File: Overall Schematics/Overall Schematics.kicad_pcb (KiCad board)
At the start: 2 copper layers, 152.4 x 152.4 mm, 28 parts, among them J1 WattMeter1_Output, J2 WattMeter2_Output, J3 Intel_Buck_Converter_Input, J4 WattMeter1_Input, J5 WattMeter2_Input, M1 Stepper_Motor_bipolar, M2 Stepper_Motor_bipolar, M3 LinActuator12V, M4 LinActuator12V, M5 LinActuator12V, M6 Motor_DC, M7 Motor_DC, M8 Motor_DC, M9 Motor_DC, SW1 SW_DPST, U1 Teensy4.1, U10 VNH52019, U12 36v4SMD, U2 36v4SMD, U3 36v4SMD, U4 VNH52019, U5 VNH52019, U6 VNH52019, U7 VNH52019, U8 VNH52019, U9 VNH52019

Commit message: flipped some screw terminals and added screw terminal
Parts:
- added M11: Stepper_Motor_bipolar, TerminalBlock:TerminalBlock_bornier-4_P5.08mm, B.Cu at (459.7, 375.9)
- BT1, BT2, J3: moved to B.Cu
- moved BT2 160.6 mm to (515.6, 429.3), turned to 90 degrees
- moved BT1 144.2 mm to (528.3, 429.3), turned to 90 degrees
- moved J5 99.7 mm to (602.0, 410.2)
- moved J3 95.6 mm to (577.9, 431.8), turned to 90 degrees
- moved M3 83.6 mm to (476.2, 459.7), turned to 180 degrees
- moved M5 48.5 mm to (459.7, 396.2), turned to 270 degrees
- moved M6 35.9 mm to (459.7, 434.3), turned to 270 degrees
- moved M9 35.6 mm to (577.9, 452.1), turned to 90 degrees
- moved M8 34.2 mm to (576.6, 416.6), turned to 90 degrees
- moved M4 33.0 mm to (458.5, 322.6), turned to 0 degrees
- moved M7 32.2 mm to (576.6, 396.2), turned to 90 degrees
- moved M2 32.2 mm to (576.6, 365.8)
- moved M1 30.6 mm to (576.6, 327.7)

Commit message: PCB Updates
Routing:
- net OUTB1_LIN: track 0.00 -> 15.2 mm
- net OUTA1_LIN: track 0.00 -> 15.2 mm
- net AOUT1_3: track 0.00 -> 12.2 mm
- net AOUT2_3: track 0.00 -> 11.9 mm
- net BOUT1_3: track 0.00 -> 10.1 mm
- net BOUT2_3: track 0.00 -> 9.06 mm
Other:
- net class Power: trace_width 0.5 -> 0.75

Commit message: PCB Updates
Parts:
- added M10: Motor_Servo, TerminalBlock:TerminalBlock_bornier-3_P5.08mm, B.Cu at (528.3, 461.0)
- added U11: ServoDriver, Custom Footprints:ServoMotorDriver, F.Cu at (539.5, 452.2)
- moved M3 1.27 mm to (475.0, 459.7)
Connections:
- U1 pad 17: LIN_SIGNAL1 -> LIN_SIGNAL3
- U1 pad 18: LIN_SIGNAL2 -> LIN_SIGNAL1
- U1 pad 19: LIN_SIGNAL3 -> LIN_SIGNAL2
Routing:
- net LIN_SIGNAL2: track 0.00 -> 170.1 mm
- net LIN_SIGNAL1: track 0.00 -> 81.7 mm
- net LIN_SIGNAL3: track 0.00 -> 61.4 mm
- net OUTB_3: track 0.00 -> 52.0 mm
- net OUTA_3: track 0.00 -> 51.0 mm
- net OUTA2_LIN: track 0.00 -> 44.6 mm
- net OUTA_4: track 0.00 -> 42.6 mm
- net OUTB_4: track 0.00 -> 41.6 mm
- net OUTB2_LIN: track 0.00 -> 38.2 mm
- net OUTB3_LIN: track 0.00 -> 22.4 mm
- net AOUT1_2: track 0.00 -> 17.2 mm
- net AOUT1_1: track 0.00 -> 15.8 mm
- net OUTA_1: track 0.00 -> 15.4 mm
- net OUTB_1: track 0.00 -> 15.4 mm
- net OUTA3_LIN: track 0.00 -> 14.2 mm
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
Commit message: did some pcb stuff
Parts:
- removed BT1: True_Spec_Battery1, Custom Footprints:AMASS_XT60-F_1x02_P7.20mm_Vertical
- removed BT2: True_Spec_Battery2, Custom Footprints:AMASS_XT60-F_1x02_P7.20mm_Vertical
- removed J4: WattMeter1_Input, TerminalBlock:TerminalBlock_bornier-2_P5.08mm
- removed J5: WattMeter2_Input, TerminalBlock:TerminalBlock_bornier-2_P5.08mm
- removed SW1: SW_DPST, Button_Switch_SMD:SW_MEC_5GSH9
- added M12: Motor_Servo, TerminalBlock:TerminalBlock_bornier-3_P5.08mm, B.Cu at (532.8, 447.7)
- J1, J2: moved to B.Cu
- moved J2 214.6 mm to (518.2, 424.8)
- moved J1 214.3 mm to (518.2, 393.1)
- moved M10 5.12 mm to (532.8, 458.5)
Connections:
- net Battery1_Positive renamed Battery2_Positive
- net Net-(M10-Pad1) renamed SS_1
- J2 pad 2: Battery1_Positive24V -> Battery2_Positive24V
- M10 pad 2: Net-(M10-Pad2) -> +5V
- M10 pad 3: Net-(M10-Pad3) -> GND
- U11 pad 13: Net-(M10-Pad3) -> GND
- U11 pad 14: Net-(U11-Pad14) -> GND
- U11 pad 2: Net-(U11-Pad2) -> SS_2
- U11 pad 7: Net-(M10-Pad2) -> +5V
- U11 pad 8: Net-(U11-Pad8) -> +5V
- U12 pad 17: Battery1_Positive24V -> Battery2_Positive24V
- U12 pad 18: Battery1_Positive24V -> Battery2_Positive24V
- U2 pad 17: Battery1_Positive24V -> Battery2_Positive24V
- U2 pad 18: Battery1_Positive24V -> Battery2_Positive24V
- U5 pad 14: Battery1_Positive24V -> Battery2_Positive24V
- U7 pad 14: Battery1_Positive24V -> Battery2_Positive24V
- U8 pad 14: Battery1_Positive24V -> Battery2_Positive24V
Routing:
- net +5V: track 0.00 -> 35.3 mm
- net LIN_SIGNAL2: track 170.1 -> 141.4 mm
- net SS_1: track 0.00 -> 25.8 mm
- net SS_2: track 0.00 -> 25.6 mm
- net OUTA2_LIN: track 44.6 -> 38.4 mm
- net OUTB2_LIN: track 38.2 -> 32.7 mm
- net AOUT1_2: track 17.2 -> 14.2 mm
- net OUTB3_LIN: track 22.4 -> 20.1 mm
- net AOUT1_1: track 15.8 -> 13.8 mm
- net OUTA3_LIN: track 14.2 -> 13.0 mm
- net OUTA_4: track 42.6 -> 41.6 mm
- net AOUT2_3: track 11.9 -> 11.2 mm
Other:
- net class Power: trace_width 0.75 -> 1
- net class Signal: trace_width 0.25 -> 0.5

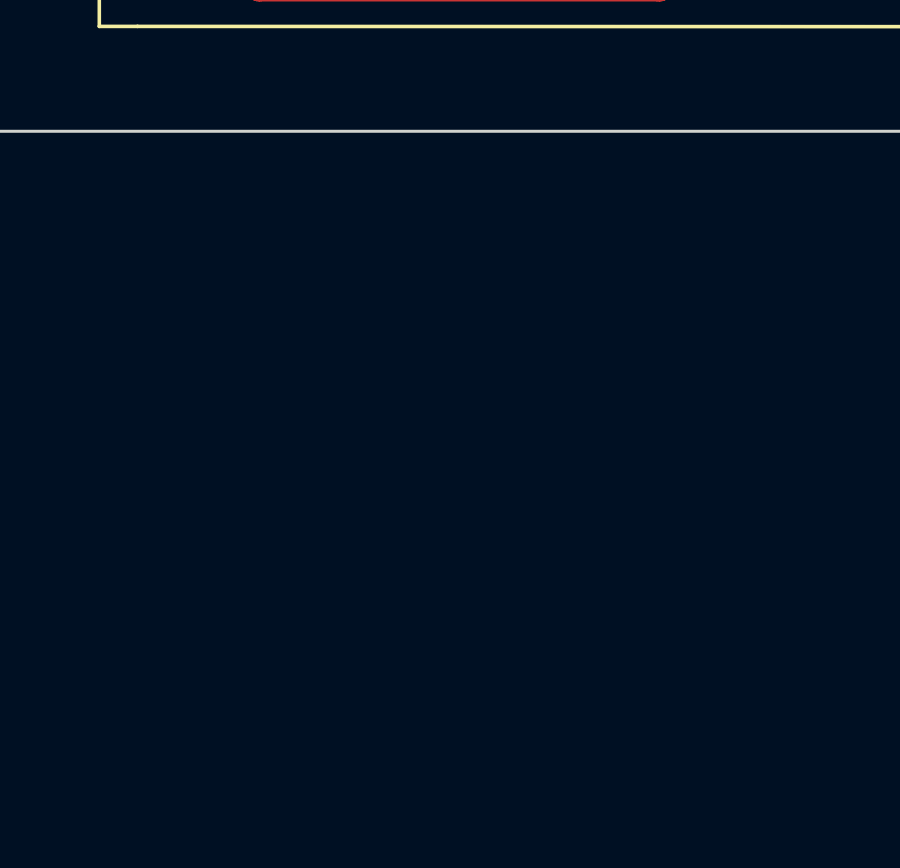
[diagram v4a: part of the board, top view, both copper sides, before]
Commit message: Added 5V buck
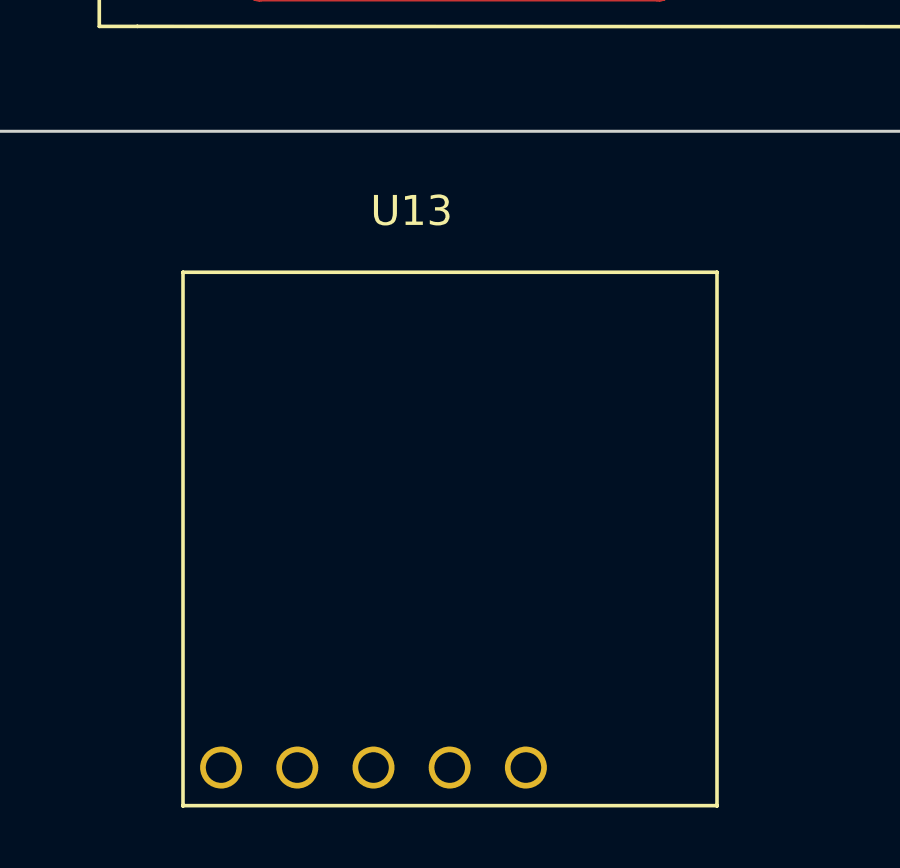
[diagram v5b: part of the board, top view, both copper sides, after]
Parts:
- added U13: D24V22F5, Custom Footprints:D24V22F5, F.Cu at (515.6, 469.3)
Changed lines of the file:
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@@
     (tracks 269)
     (zones 0)
-    (modules 27)
+    (modules 28)
     (nets 159)
   )
@@
     )
   )
+  (module "Custom Footprints:D24V22F5" (layer F.Cu)
+    (at 515.62 469.265)
+    (fp_text reference U13 (at 0 0.5) (layer F.SilkS)
+      (effects (font (size 1 1) (thickness 0.15)))
+    )
+    (fp_text value D24V22F5 (at 0 -0.5) (layer F.Fab)
+      (effects (font (size 1 1) (thickness 0.15)))
+    )
+    (fp_line (start -7.62 20.32) (end 10.18 20.32) (layer F.SilkS) (width 0.12))
+    (fp_line (start 10.18 2.54) (end 10.18 20.34) (layer F.SilkS) (width 0.12))
+    (fp_line (start -7.62 2.54) (end 10.18 2.54) (layer F.SilkS) (width 0.12))
+    (fp_line (start -7.62 2.54) (end -7.62 20.34) (layer F.SilkS) (width 0.12))
+    (pad 1 thru_hole circle (at -6.35 19.05) (size 1.4 1.4) (drill 1.02) (layers *.Cu *.Mask))
+    (pad 2 thru_hole circle (at -3.81 19.05) (size 1.4 1.4) (drill 1.02) (layers *.Cu *.Mask))
+    (pad 3 thru_hole circle (at -1.27 19.05) (size 1.4 1.4) (drill 1.02) (layers *.Cu *.Mask))
+    (pad 4 thru_hole circle (at 1.27 19.05) (size 1.4 1.4) (drill 1.02) (layers *.Cu *.Mask))
+    (pad 5 thru_hole circle (at 3.81 19.05) (size 1.4 1.4) (drill 1.02) (layers *.Cu *.Mask))
+  )
   (gr_line (start 592.074 314.706) (end 592.1 467.106) (layer Edge.Cuts) (width 0.1))

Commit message: PCB is basically done, going to check stuff again before ordering though
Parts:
- moved J2 105.1 mm to (543.6, 322.8)
- moved J1 73.7 mm to (495.8, 322.8)
- moved U13 33.5 mm to (497.2, 441.3)
- moved M10 5.72 mm to (538.5, 458.5)
- moved M12 5.72 mm to (538.5, 447.7)
- moved U11 5.72 mm to (545.2, 452.2)
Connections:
- J3 pad 1: Battery2_Positive -> Battery2_Positive24V
- U10 pad 14: Battery1_Positive24V -> Battery2_Positive24V
- U12 pad 17: Battery2_Positive24V -> Battery1_Positive24V
- U12 pad 18: Battery2_Positive24V -> Battery1_Positive24V
- U13 pad 1: (no net) -> Net-(U13-Pad1)
- U13 pad 2: (no net) -> Net-(U13-Pad2)
- U13 pad 3: (no net) -> Battery1_Positive24V
- U13 pad 4: (no net) -> GND
- U13 pad 5: (no net) -> +5V
- U3 pad 17: Battery1_Positive24V -> Battery2_Positive24V
- U3 pad 18: Battery1_Positive24V -> Battery2_Positive24V
- U5 pad 14: Battery2_Positive24V -> Battery1_Positive24V
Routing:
- net +3V3: track 0.00 -> 475.4 mm, vias 0 -> 1
- net Battery1_Positive24V: track 0.00 -> 293.3 mm
- net Battery2_Positive24V: track 0.00 -> 249.6 mm
- net +5V: track 35.3 -> 50.6 mm
- net PWM_4: track 38.3 -> 43.7 mm
- net DIR_1: track 30.6 -> 36.0 mm
- net STEP_1: track 30.6 -> 35.4 mm
- net PWM_7: track 26.9 -> 29.7 mm
- net INA_7: track 28.0 -> 30.5 mm
- net OUTB2_LIN: track 32.7 -> 31.2 mm
- net LIN_SIGNAL2: track 141.4 -> 139.9 mm
- net INA_4: track 35.9 -> 37.1 mm
- net INB_4: track 25.8 -> 27.0 mm
- net INA_3: track 50.4 -> 49.3 mm
- net INB_3: track 67.5 -> 66.4 mm
- added copper zone on F.Cu, net GND
- added copper zone on B.Cu, net PWR_GND
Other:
- net class Power: via_dia 0.8 -> 1.2; via_drill 0.4 -> 0.8

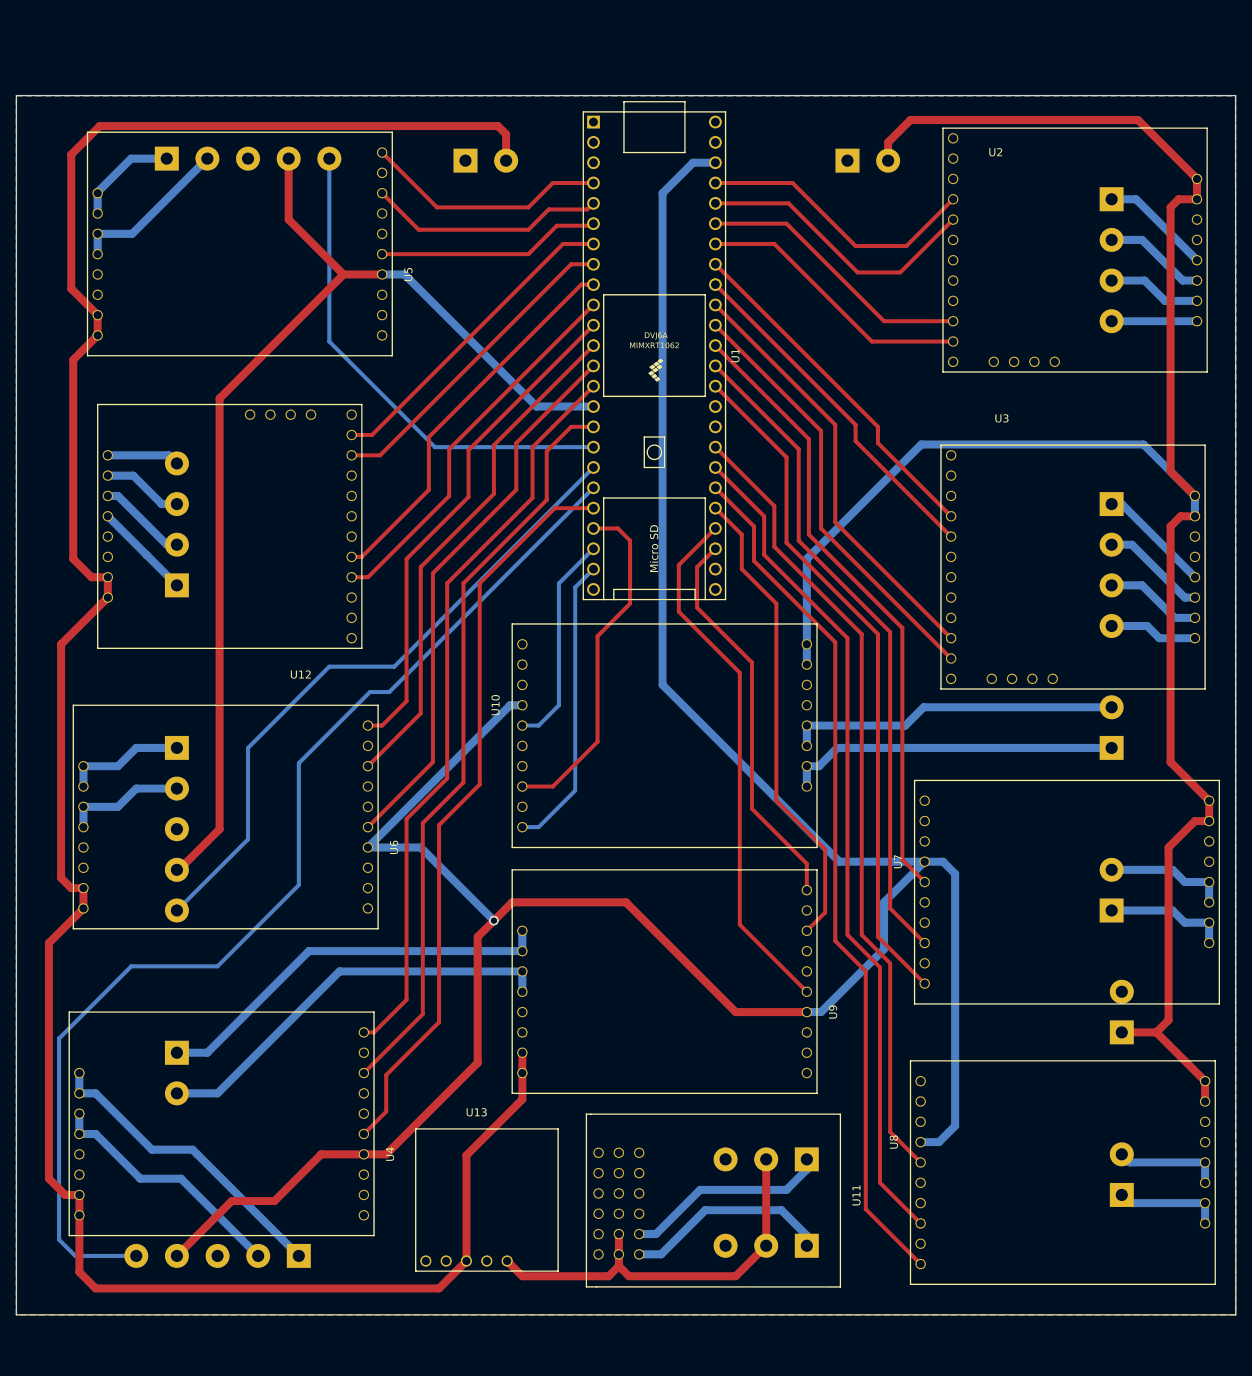
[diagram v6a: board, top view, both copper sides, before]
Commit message: Added mounting, add to make board a bit bigger. Changed servo screw terminal pitch to 2.54mm
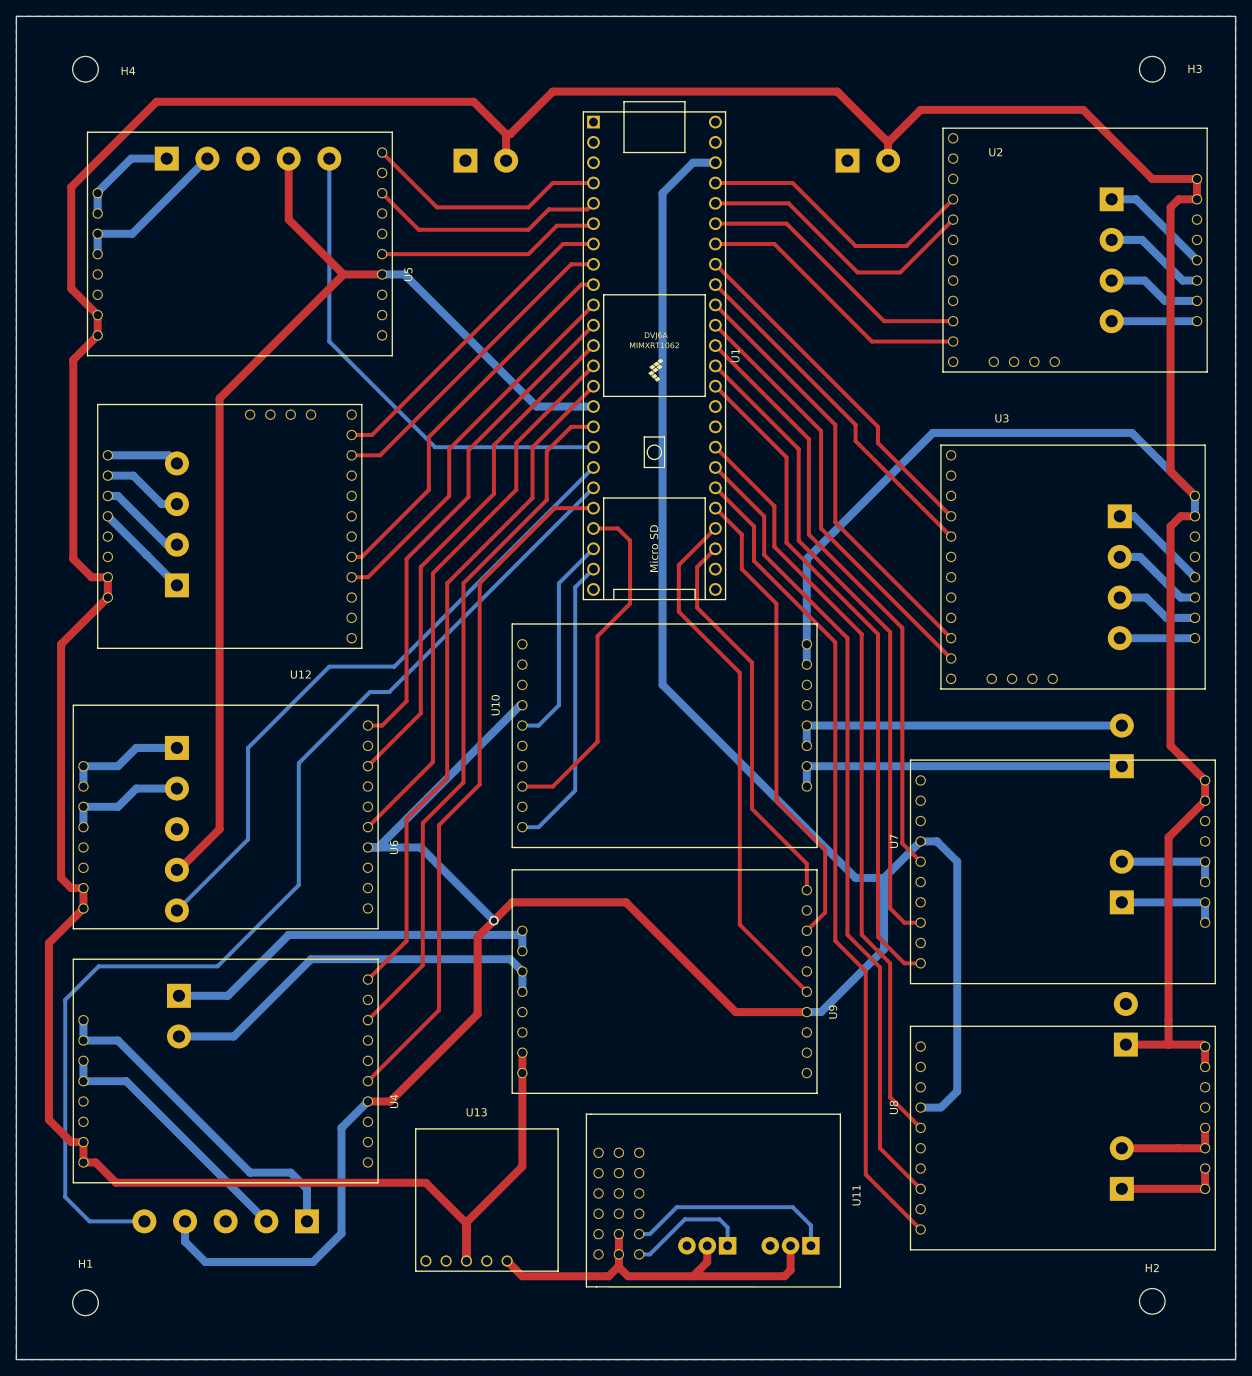
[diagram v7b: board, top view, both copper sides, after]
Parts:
- added H1: MountingHole, MountingHole:MountingHole_3.2mm_M3, F.Cu at (448.3, 465.6)
- added H2: MountingHole, MountingHole:MountingHole_3.2mm_M3, F.Cu at (581.7, 465.5)
- added H3: MountingHole, MountingHole:MountingHole_3.2mm_M3, F.Cu at (581.7, 311.4)
- added H4: MountingHole, MountingHole:MountingHole_3.2mm_M3, F.Cu at (448.3, 311.4)
- M10, M12: footprint TerminalBlock:TerminalBlock_bornier-3_P5.08mm -> Custom Footprints:TerminalBlock_2.54_1x03_P2.54mm_Horizontal
- moved M12 10.8 mm to (539.0, 458.5)
- moved M10 9.91 mm to (528.6, 458.5)
- moved M6 7.12 mm to (460.0, 427.2)
- moved U4 6.62 mm to (487.4, 440.4)
- moved M3 4.44 mm to (476.0, 455.4)
- moved U8 4.32 mm to (548.9, 441.2)
- moved M7 2.62 mm to (577.9, 398.5)
- moved U7 2.59 mm to (548.9, 407.9)
- moved M2 1.83 mm to (577.6, 367.3)
- moved M8 1.63 mm to (577.9, 415.5)
- moved J3 1.61 mm to (578.4, 433.3)
- moved M9 0.76 mm to (577.9, 451.4)
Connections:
- net +3V3 renamed 3.3V
- J2 pad 2: Battery2_Positive24V -> Battery1_Positive24V
- J3 pad 1: Battery2_Positive24V -> Battery1_Positive24V
- U10 pad 14: Battery2_Positive24V -> Battery1_Positive24V
- U2 pad 17: Battery2_Positive24V -> Battery1_Positive24V
- U2 pad 18: Battery2_Positive24V -> Battery1_Positive24V
- U3 pad 17: Battery2_Positive24V -> Battery1_Positive24V
- U3 pad 18: Battery2_Positive24V -> Battery1_Positive24V
- U7 pad 14: Battery2_Positive24V -> Battery1_Positive24V
- U8 pad 14: Battery2_Positive24V -> Battery1_Positive24V
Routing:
- net Battery1_Positive24V: track 293.3 -> 585.9 mm
- net Battery2_Positive24V: track 249.6 -> 0.00 mm
- net SS_1: track 25.8 -> 15.6 mm
- net INA_6: track 93.4 -> 85.8 mm
- net PWM_6: track 94.3 -> 87.5 mm
- net INB_6: track 92.9 -> 86.1 mm
- net INA_2: track 107.7 -> 103.3 mm
- net PWM_2: track 105.1 -> 100.8 mm
- net INB_2: track 100.0 -> 95.7 mm
- net OUTA2_LIN: track 38.4 -> 42.2 mm
- net 3.3V: track 475.4 -> 479.0 mm
- net INB_1: track 77.9 -> 75.1 mm
- net LIN_SIGNAL2: track 139.9 -> 137.3 mm
- net OUTA_1: track 15.4 -> 13.0 mm
- net OUTB_1: track 15.4 -> 13.0 mm
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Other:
- board size 152.4 x 152.4 mm -> 152.4 x 167.9 mm
